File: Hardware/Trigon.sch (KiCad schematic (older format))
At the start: 110 parts, among them J1 TYPE-C-31-M12_13, J2 TYPE-C-31-M12_13, J3 Conn_01x05, SW1 SW_Push, SW2 Rotary_Encoder_Switch, U1 ATmega32U4-AU, U2 USBLC6-2SC6, U3 CY7C65632-28LTXCT, U4 USBLC6-2SC6, Y1 16MHz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

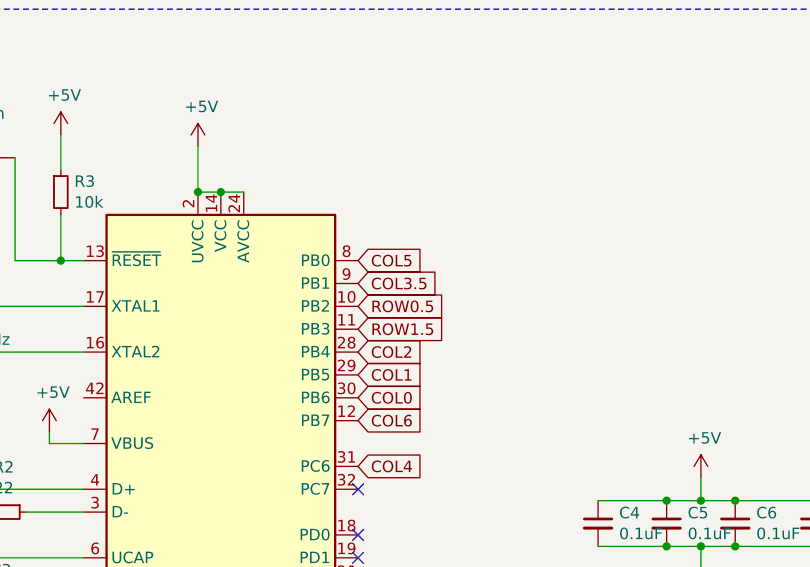
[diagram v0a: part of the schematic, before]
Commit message: Cleanup of incorrect pins
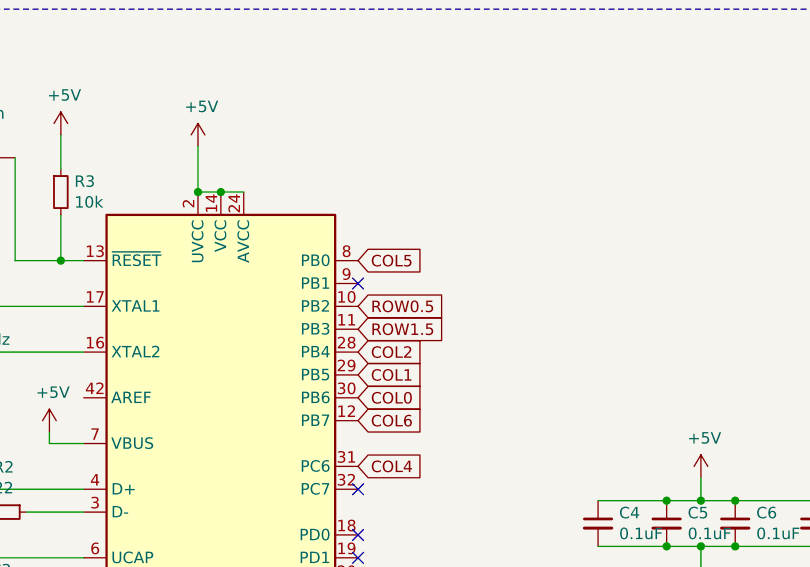
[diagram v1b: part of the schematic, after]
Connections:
- net COL3.5: no longer names the net of U1.9 (PB1)
- no-connect marks 19 -> 20
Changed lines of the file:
@@
 	1    0    0    -1
 $EndComp
-Text GLabel 3650 2150 2    50   Input ~ 0
-COL3.5
 Text GLabel 20450 3350 0    50   Input ~ 0
 ROW1.5
@@
 Connection ~ 19300 1900
 Connection ~ 19300 2700
+NoConn ~ 3650 2150
 $EndSCHEMATC

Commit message: lots of changes
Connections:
- net D2_D+ renamed D4_D+
- net D2_D- renamed D4_D-
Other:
- note added: "downstream jst connector"
- moved on the sheet: C4, C5, C6, C7, J3, R11, R12, R13, R14, R15, R16, R5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

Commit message: preping for pcbway
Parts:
- added H2: Logo, Trigon:back, symbol Mechanical:MountingHole
- added H3: Logo, Trigon:backside, symbol Mechanical:MountingHole
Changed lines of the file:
@@
 Wire Notes Line
 	17650 14100 17650 12800
+$Comp
+L Mechanical:MountingHole H2
+U 1 1 6080F99B
+P 2150 14300
+F 0 "H2" H 2250 14346 50  0000 L CNN
+F 1 "Logo" H 2250 14255 50  0000 L CNN
+F 2 "Trigon:back" H 2150 14300 50  0001 C CNN
+F 3 "~" H 2150 14300 50  0001 C CNN
+	1    2150 14300
+	1    0    0    -1
+$EndComp
+$Comp
+L Mechanical:MountingHole H3
+U 1 1 6084B3F1
+P 3300 14300
+F 0 "H3" H 3400 14346 50  0000 L CNN
+F 1 "Logo" H 3400 14255 50  0000 L CNN
+F 2 "Trigon:backside" H 3300 14300 50  0001 C CNN
+F 3 "~" H 3300 14300 50  0001 C CNN
+	1    3300 14300
+	1    0    0    -1
+$EndComp
 $EndSCHEMATC
